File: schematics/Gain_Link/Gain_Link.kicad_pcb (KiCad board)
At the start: 2 copper layers, 78.2 x 96 mm, 27 parts, among them IC1 AD8221TRMZ-EP, IC2 AD8221TRMZ-EP, IC3 AD8221TRMZ-EP, IC4 AD8221TRMZ-EP, J1 PCIE-036-02-X-D-TH, J2 Conn_02x03_Odd_Even, J3 Conn_02x03_Odd_Even

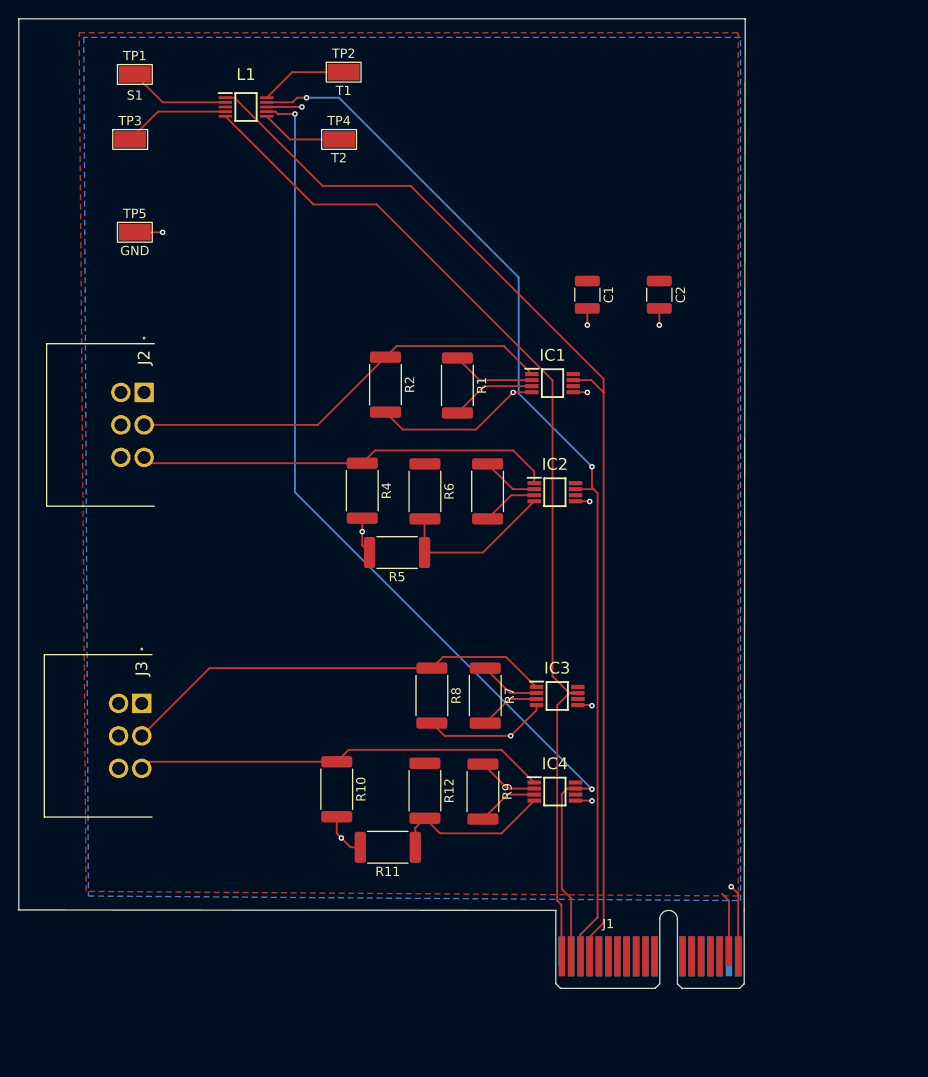
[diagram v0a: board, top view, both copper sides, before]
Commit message: Measured out Board Components Added TVS Diodes Edited to be 4 layers (currently) 	-Top: Signals 	-Mid1: GND 	-Mid2: ?? 	-Bottom: +12V
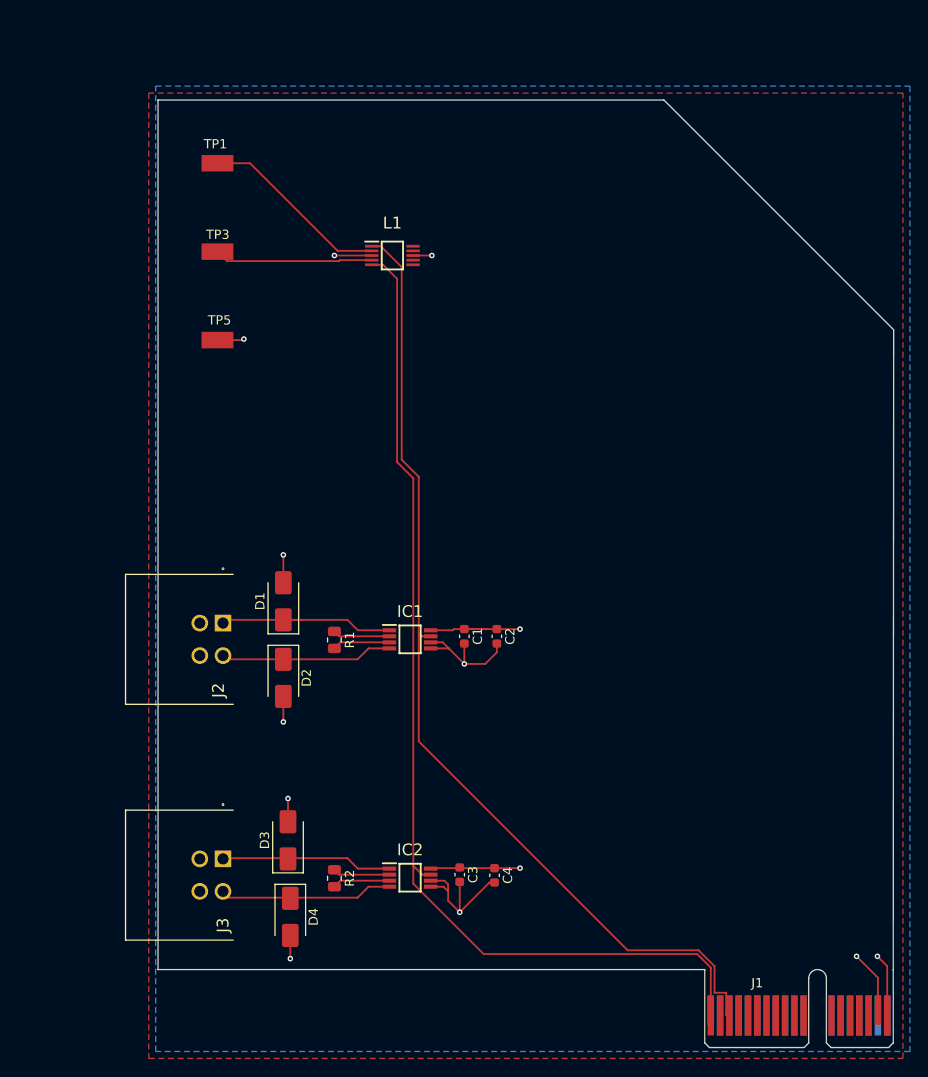
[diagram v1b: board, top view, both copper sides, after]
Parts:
- removed IC3, IC4: AD8221TRMZ-EP, Link_Footprints:AD8221TRMZ-EP
- removed R10, R11, R12, R4, R5, R6: R, Resistor_SMD:R_2512_6332Metric
- removed R3: R_{g2}, Resistor_SMD:R_2512_6332Metric
- removed R7: R_{g3}, Resistor_SMD:R_2512_6332Metric
- removed R8: R_{shunt}, Resistor_SMD:R_2512_6332Metric
- removed R9: R_{g4}, Resistor_SMD:R_2512_6332Metric
- removed TP2: T1, Link_Footprints:KEYSTONE_5017
- removed TP4: T2, Link_Footprints:KEYSTONE_5017
- added C3: 0.1 uF, Capacitor_SMD:C_0603_1608Metric, F.Cu at (125.0, 119.0)
- added C4: 10 uF, Capacitor_SMD:C_0603_1608Metric, F.Cu at (128.8, 119.0)
- added D1: SMAJ20A, Diode_SMD:D_SMA, F.Cu at (106.0, 89.5)
- added D2: SMAJ20A, Diode_SMD:D_SMA, F.Cu at (106.0, 97.8)
- added D3: SMAJ20A, Diode_SMD:D_SMA, F.Cu at (106.5, 115.2)
- added D4: SMAJ20A, Diode_SMD:D_SMA, F.Cu at (106.8, 123.5)
- C1, C2: footprint Capacitor_SMD:C_1210_3225Metric -> Capacitor_SMD:C_0603_1608Metric
- IC1, IC2: footprint Link_Footprints:AD8221TRMZ-EP -> Link Footprints:AD8221TRMZ
- J2, J3: value Conn_02x03_Odd_Even -> Conn_02x02_Odd_Even; footprint Link_Footprints:1818517 -> Link Footprints:PC-1053864
- L1: footprint Link_Footprints:AD8244ARMZ -> Link Footprints:AD8244ARMZ
- R1: value R_{g1} -> 330; footprint Resistor_SMD:R_2512_6332Metric -> Resistor_SMD:R_0805_2012Metric
- R2: value R_{shunt} -> 330; footprint Resistor_SMD:R_2512_6332Metric -> Resistor_SMD:R_0805_2012Metric
- TP1, TP3, TP5: footprint Link_Footprints:KEYSTONE_5017 -> Link Footprints:Keystone_5017
- moved R2 53.5 mm to (111.5, 119.3)
- moved IC2 44.4 mm to (119.7, 119.3)
- moved C2 40.7 mm to (129.0, 93.3)
- moved C1 39.1 mm to (125.5, 93.3)
- moved J2 36.2 mm to (101.6, 101.6)
- moved IC1 31.6 mm to (119.7, 93.6)
- moved R1 30.4 mm to (111.5, 93.7)
- moved J3 28.6 mm to (101.6, 127.0)
- moved L1 22.5 mm to (117.8, 52.2)
- moved J1 15.5 mm to (151.4, 129.2)
- moved TP3 15.2 mm to (96.9, 53.0)
- moved TP5 14.5 mm to (96.9, 62.5)
- moved TP1 12.8 mm to (96.9, 43.5)
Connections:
- IC1 pad 4: GND -> /S_{1-}
- IC1 pad 6: /+2V5 -> GND
- IC2 pad 1: /T_{1-} -> /S_{2+}
- IC2 pad 4: Net-(IC2-+IN) -> /S_{2-}
- IC2 pad 6: /V_{ref} -> GND
- IC2 pad 7: /T_{1out} -> /S_{2out}
- IC2 pad 8: unconnected-(IC2-+VS-Pad8) -> +12V
- J1 pad B15: unconnected-(J1-PadB15) -> -12V
- J1 pad B2: /T_{2out} -> unconnected-(J1-PadB2)
- J1 pad B3: /T_{1out} -> /S_{1out}
- J1 pad B4: /S_{1out} -> unconnected-(J1-PadB4)
- J2 pad 1: +12V -> /S_{1+}
- J2 pad 2: /S_{1+} -> /S_{1-}
- J2 pad 3: /T_{1-} -> +5V
- J2 pad 4: +12V -> GND
- J3 pad 1: +12V -> /S_{2+}
- J3 pad 2: /S_{2+} -> /S_{2-}
- J3 pad 3: /T_{2-} -> +5V
- J3 pad 4: +12V -> GND
- L1 pad 10: /T_{1test} -> unconnected-(L1-IND-Pad10)
- L1 pad 6: /T_{2test} -> unconnected-(L1-INC-Pad6)
- L1 pad 7: /T_{2out} -> unconnected-(L1-OUTC-Pad7)
- L1 pad 9: /T_{1out} -> unconnected-(L1-OUTD-Pad9)
- R2 pad 1: /S_{1+} -> Net-(IC2-RG_1)
- R2 pad 2: GND -> Net-(IC2-RG_2)
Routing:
- net /T_{1out}: track 114.8 -> 0.00 mm, vias 2 -> 0
- net /T_{2out}: track 110.6 -> 0.00 mm, vias 2 -> 0
- net /T_{1-}: track 45.0 -> 0.00 mm
- net /T_{2-}: track 44.6 -> 0.00 mm
- net /S_{2+}: track 47.4 -> 18.0 mm
- net /S_{1+}: track 46.5 -> 20.5 mm
- net +12V: track 6.76 -> 31.9 mm, vias 0 -> 4
- net /S_{1-}: track 0.00 -> 18.6 mm
- net /S_{2-}: track 0.00 -> 18.0 mm
- net Net-(IC2-+IN): track 17.7 -> 0.00 mm
- net Net-(IC4-+IN): track 17.5 -> 0.00 mm
- net /S_{1out}: track 119.9 -> 106.3 mm
- net GND: track 65.7 -> 52.2 mm, vias 13 -> 9
- net /S_{1test}: track 11.0 -> 20.5 mm
- net /T_{1test}: track 9.44 -> 0.00 mm
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- added copper zone on F.Cu, net (none)
- added copper zone on B.Cu, net +12V
- added copper zone on In1.Cu, net GND
- removed copper zone on F.Cu, net +12V
- removed copper zone on B.Cu, net GND
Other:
- board size 78.2 x 96 mm -> 79.2 x 93.7 mm
- copper layers 2 -> 4
- board text removed: "OATS Center Shunt-Link v1 (10/13/2025) abalmos@purdue.edu"

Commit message: Replaced AD8221 with INA849, made board smaller
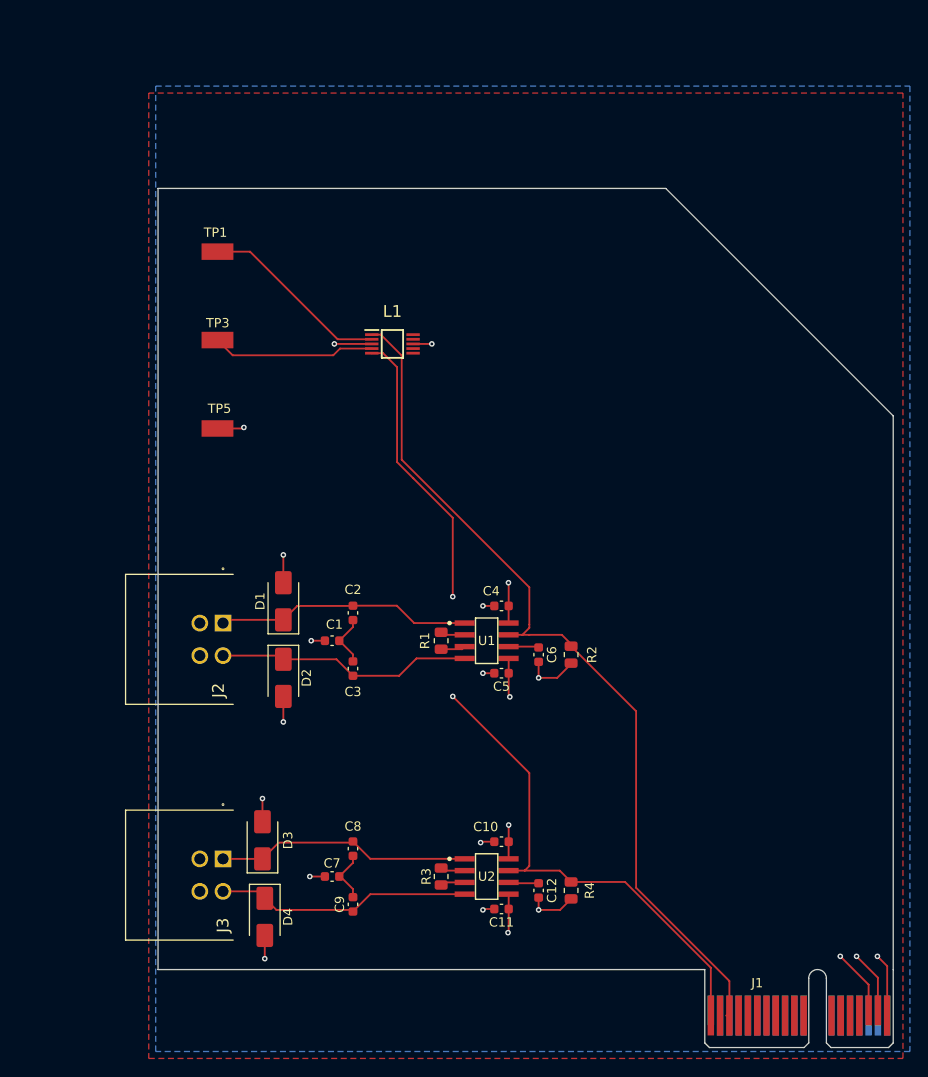
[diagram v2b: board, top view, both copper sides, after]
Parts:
- removed IC1, IC2: AD8221TRMZ-EP, Link Footprints:AD8221TRMZ
- added C10: 0.1 uF, Capacitor_SMD:C_0603_1608Metric, F.Cu at (129.5, 115.4)
- added C11: 0.1 uF, Capacitor_SMD:C_0603_1608Metric, F.Cu at (129.5, 122.7)
- added C12: 100pF, Capacitor_SMD:C_0603_1608Metric, F.Cu at (133.5, 120.7)
- added C5: 0.1 uF, Capacitor_SMD:C_0603_1608Metric, F.Cu at (129.5, 97.2)
- added C6: 100pF, Capacitor_SMD:C_0603_1608Metric, F.Cu at (133.5, 95.2)
- added C7: 47pF, Capacitor_SMD:C_0603_1608Metric, F.Cu at (111.2, 119.2)
- added C8: 470pF, Capacitor_SMD:C_0603_1608Metric, F.Cu at (113.5, 116.2)
- added C9: 470pF, Capacitor_SMD:C_0603_1608Metric, F.Cu at (113.5, 122.2)
- added R3: 1, Resistor_SMD:R_0805_2012Metric, F.Cu at (123.0, 119.2)
- added R4: 10k, Resistor_SMD:R_0805_2012Metric, F.Cu at (137.0, 120.7)
- added U1: INA849D, Link Footprints:INA849, F.Cu at (127.9, 93.8)
- added U2: INA849D, Link Footprints:INA849, F.Cu at (127.9, 119.2)
- C1: value 0.1 uF -> 47pF
- C2: value 10 uF -> 470pF
- C3: value 0.1 uF -> 470pF
- C4: value 10 uF -> 0.1 uF
- R1: value 330 -> 1
- R2: value 330 -> 10k
- moved R2 35.1 mm to (137.0, 95.2), turned to 90 degrees
- moved C4 29.0 mm to (129.5, 90.0), turned to 180 degrees
- moved C3 25.0 mm to (113.5, 96.8), turned to 90 degrees
- moved C2 15.7 mm to (113.5, 90.8), turned to 90 degrees
- moved C1 14.3 mm to (111.2, 93.8), turned to 0 degrees
- moved R1 11.5 mm to (123.0, 93.8)
- moved TP5 9.53 mm to (96.9, 72.0)
- moved L1 9.52 mm to (117.8, 61.8)
- moved TP1 9.52 mm to (96.9, 53.0)
- moved TP3 9.52 mm to (96.9, 62.5)
- moved D3 2.75 mm to (103.8, 115.2)
- moved D4 2.75 mm to (104.0, 123.5)
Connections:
- C1 pad 1: +12V -> GND
- C1 pad 2: GND -> Net-(C1-Pad2)
- C2 pad 1: +12V -> Net-(C1-Pad2)
- C2 pad 2: GND -> /S_{1-}
- C3 pad 1: +12V -> /S_{1+}
- C3 pad 2: GND -> Net-(C1-Pad2)
- D1 pad 1: /S_{1+} -> /S_{1-}
- D2 pad 1: /S_{1-} -> /S_{1+}
- D3 pad 1: /S_{2+} -> /S_{2-}
- D4 pad 1: /S_{2-} -> /S_{2+}
- J1 pad B15: -12V -> unconnected-(J1-PadB15)
- J1 pad B16: unconnected-(J1-PadB16) -> -12V
- J2 pad 1: /S_{1+} -> /S_{1-}
- J2 pad 2: /S_{1-} -> /S_{1+}
- J3 pad 1: /S_{2+} -> /S_{2-}
- J3 pad 2: /S_{2-} -> /S_{2+}
- R2 pad 1: Net-(IC2-RG_1) -> GND
- R2 pad 2: Net-(IC2-RG_2) -> /S_{1out}
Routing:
- net /S_{2out}: track 112.5 -> 95.0 mm, vias 0 -> 2
- net -12V: track 0.00 -> 16.0 mm, vias 0 -> 3
- net +12V: track 31.9 -> 18.8 mm
- net /S_{1out}: track 106.3 -> 94.8 mm
- net GND: track 52.2 -> 41.8 mm, vias 9 -> 15
- net /S_{2+}: track 18.0 -> 27.7 mm
- net /S_{2-}: track 18.0 -> 27.6 mm
- net /S_{1-}: track 18.6 -> 28.1 mm
- net /S_{1+}: track 20.5 -> 28.3 mm
- net -10V: track 0.00 -> 6.55 mm
- net Net-(IC2-RG_2): track 6.19 -> 0.00 mm
- net Net-(IC2-RG_1): track 6.14 -> 0.00 mm
- net Net-(C7-Pad2): track 0.00 -> 5.75 mm
- net Net-(C1-Pad2): track 0.00 -> 5.67 mm
- net Net-(R1-Pad2): track 6.19 -> 2.65 mm
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- added copper zone on In2.Cu, net -12V
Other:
- board size 79.2 x 93.7 mm -> 79.2 x 84.2 mm
